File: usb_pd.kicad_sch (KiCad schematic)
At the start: 42 parts, among them J1 USB-C_GCT_USB4105-GF-A, J2 JST_SH_1x4_SM04B-SRSS-TB-LF-SN, Q1 SQS401EN-T1_BE3, U1 STUSB4500_QFN, U5 TVS2200DRVR, U6 TPD4E02B04DQA, U7 TVS2200DRVR, U8 TVS2200DRVR

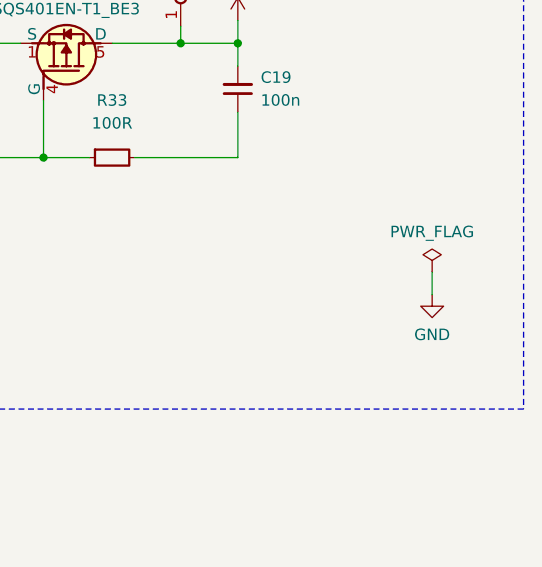
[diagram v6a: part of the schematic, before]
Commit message: [#57764] ADD GND testpoint
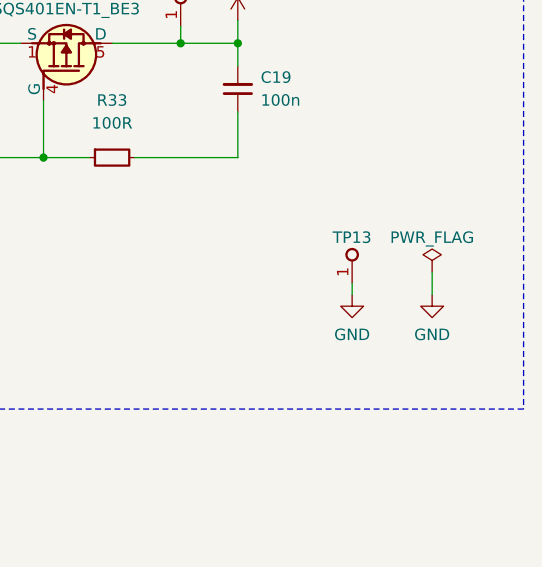
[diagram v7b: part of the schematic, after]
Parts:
- added TP13: TP_0.75mm_SMD, antmicro-footprints:TP_SMD_0.75mm, symbol antmicroTestPoints:TP_0.75mm_SMD
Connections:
- net GND: now also TP13.1
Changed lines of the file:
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@@
     (stroke (width 0) (type default))
   )
+  (wire (pts (xy 339.09 87.63) (xy 339.09 88.9))
+    (stroke (width 0) (type default))
+  )
   (wire (pts (xy 260.35 127) (xy 260.35 130.81))
     (stroke (width 0) (type default))
@@
     )
   )
+  (symbol (lib_id "antmicroTestPoints:TP_0.75mm_SMD") (at 339.09 87.63 90) (unit 1)
+    (in_bom no) (on_board yes) (dnp no)
+    (property "Reference" "TP13" (at 339.09 82.55 90)
+      (effects (font (size 1.27 1.27) (thickness 0.15)))
+    )
+    (property "Value" "TP_0.75mm_SMD" (at 342.9 76.835 0)
+      (effects (font (size 1.27 1.27) (thickness 0.15)) (justify left bottom) hide)
+    )
+    (property "Footprint" "antmicro-footprints:TP_SMD_0.75mm" (at 345.44 76.835 0)
+      (effects (font (size 1.27 1.27) (thickness 0.15)) (justify left bottom) hide)
+    )
+    (property "Datasheet" "" (at 351.79 69.85 0)
+      (effects (font (size 1.27 1.27) (thickness 0.15)) (justify left bottom) hide)
+    )
+    (property "MPN" "" (at 350.52 76.835 0)
+      (effects (font (size 1.27 1.27) (thickness 0.15)) (justify left bottom) hide)
+    )
+    (property "Manufacturer" "" (at 345.44 76.835 0)
+      (effects (font (size 1.27 1.27) (thickness 0.15)) (justify left bottom) hide)
+    )
+    (property "Author" "Antmicro" (at 347.98 76.835 0)
+      (effects (font (size 1.27 1.27) (thickness 0.15)) (justify left bottom) hide)
+    )
+    (property "License" "Apache-2.0" (at 350.52 76.835 0)
+      (effects (font (size 1.27 1.27) (thickness 0.15)) (justify left bottom) hide)
+    )
+    (pin "1")
+    (instances
+      (project "USB-C-power-adapter"
+        (path "/8da33aa8-79ed-467a-95ed-bf58aa0d1db6/344e016f-20ec-4e27-ac78-d9a1e9a3533b"
+          (reference "TP13") (unit 1)
+        )
+      )
+    )
+  )
   (symbol (lib_id "antmicropower:VBUS") (at 106.68 81.28 0) (mirror y) (unit 1)
     (in_bom yes) (on_board yes) (dnp no) (fields_autoplaced)
@@
   )
   (symbol (lib_id "antmicropower:PWR_FLAG") (at 347.98 86.36 0) (unit 1)
-    (in_bom yes) (on_board yes) (dnp no) (fields_autoplaced)
+    (in_bom yes) (on_board yes) (dnp no)
     (property "Reference" "#FLG01" (at 347.98 84.455 0)
       (effects (font (size 1.27 1.27)) hide)
     )
-    (property "Value" "PWR_FLAG" (at 347.98 81.915 0)
+    (property "Value" "PWR_FLAG" (at 347.98 82.55 0)
       (effects (font (size 1.27 1.27)))
     )
@@
         )
       )
+    )
+  )
+  (symbol (lib_id "antmicropower:GND") (at 339.09 88.9 0) (mirror y) (unit 1)
+    (in_bom yes) (on_board yes) (dnp no) (fields_autoplaced)
+    (property "Reference" "#PWR04" (at 330.2 91.44 0)
+      (effects (font (size 1.27 1.27) (thickness 0.15)) (justify left bottom) hide)
+    )
+    (property "Value" "GND" (at 339.09 93.345 0)
+      (effects (font (size 1.27 1.27) (thickness 0.15)))
+    )
+    (property "Footprint" "" (at 330.2 96.52 0)
+      (effects (font (size 1.27 1.27) (thickness 0.15)) (justify left bottom) hide)
+    )
+    (property "Datasheet" "" (at 330.2 101.6 0)
+      (effects (font (size 1.27 1.27) (thickness 0.15)) (justify left bottom) hide)
+    )
+    (property "Author" "Antmicro" (at 330.2 96.52 0)
+      (effects (font (size 1.27 1.27) (thickness 0.15)) (justify left bottom) hide)
+    )
+    (property "License" "Apache-2.0" (at 330.2 99.06 0)
+      (effects (font (size 1.27 1.27) (thickness 0.15)) (justify left bottom) hide)
+    )
+    (pin "1")
+    (instances
+      (project "USB-C-power-adapter"
+        (path "/8da33aa8-79ed-467a-95ed-bf58aa0d1db6/344e016f-20ec-4e27-ac78-d9a1e9a3533b"
+          (reference "#PWR04") (unit 1)
+        )
+      )

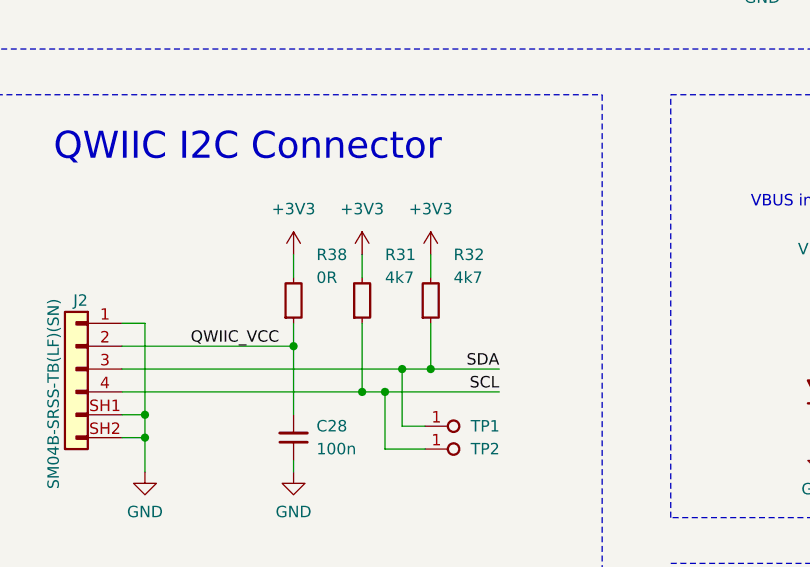
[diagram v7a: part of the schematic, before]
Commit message: [#57225] Improve Vbus, add output caps to layout
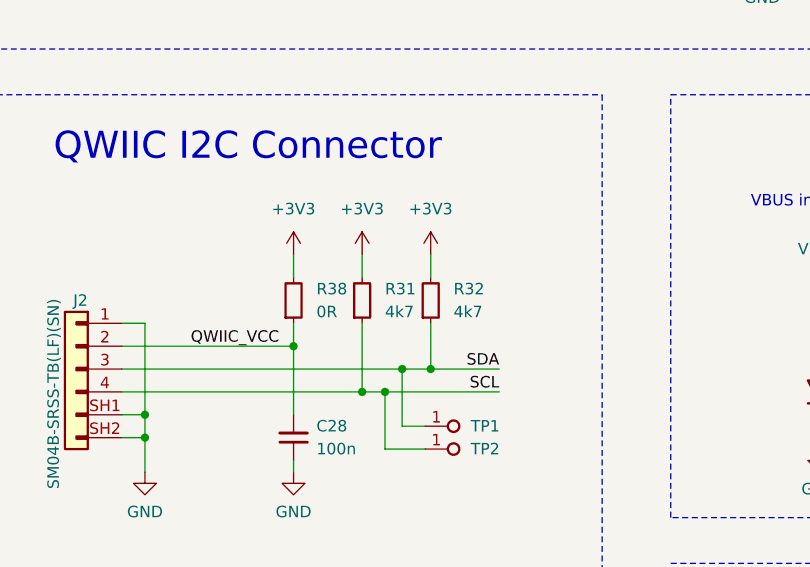
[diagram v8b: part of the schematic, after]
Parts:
- removed R38: R_0R_0603, antmicro-footprints:R_0603_1608Metric, symbol antmicroResistors0603:R_0R_0603
- added R38: R_0R_0402, antmicro-footprints:R_0402_1005Metric, symbol antmicroResistors0402:R_0R_0402
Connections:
- net +3V3: now also R38.2
- net QWIIC_VCC: now also R38.1
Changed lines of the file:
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@@
   )
   (symbol (lib_id "antmicroResistors0402:R_4k7_0402") (at 171.45 132.08 90) (unit 1)
-    (in_bom yes) (on_board yes) (dnp no)
-    (property "Reference" "R31" (at 173.99 124.46 90)
+    (in_bom yes) (on_board yes) (dnp no) (fields_autoplaced)
+    (property "Reference" "R31" (at 173.99 128.27 90)
       (effects (font (size 1.27 1.27) (thickness 0.15)) (justify right))
     )
@@
       (effects (font (size 1.27 1.27) (thickness 0.15)) (justify left bottom) hide)
     )
-    (property "Val" "4k7" (at 173.99 127 90)
+    (property "Val" "4k7" (at 173.99 130.81 90)
       (effects (font (size 1.27 1.27) (thickness 0.15)) (justify right))
     )
@@
   )
   (symbol (lib_id "antmicroResistors0402:R_4k7_0402") (at 179.07 132.08 90) (unit 1)
-    (in_bom yes) (on_board yes) (dnp no)
-    (property "Reference" "R32" (at 181.61 124.46 90)
+    (in_bom yes) (on_board yes) (dnp no) (fields_autoplaced)
+    (property "Reference" "R32" (at 181.61 128.27 90)
       (effects (font (size 1.27 1.27) (thickness 0.15)) (justify right))
     )
@@
       (effects (font (size 1.27 1.27) (thickness 0.15)) (justify left bottom) hide)
     )
-    (property "Val" "4k7" (at 181.61 127 90)
+    (property "Val" "4k7" (at 181.61 130.81 90)
       (effects (font (size 1.27 1.27) (thickness 0.15)) (justify right))
     )
@@
         (path "/8da33aa8-79ed-467a-95ed-bf58aa0d1db6/344e016f-20ec-4e27-ac78-d9a1e9a3533b"
           (reference "J2") (unit 1)
-        )
-      )
-    )
-  )
-  (symbol (lib_id "antmicroResistors0603:R_0R_0603") (at 163.83 132.08 90) (unit 1)
-    (in_bom yes) (on_board yes) (dnp no)
-    (property "Reference" "R38" (at 166.37 124.46 90)
-      (effects (font (size 1.27 1.27) (thickness 0.15)) (justify right))
-    )
-    (property "Value" "R_0R_0603" (at 176.53 111.76 0)
-      (effects (font (size 1.27 1.27) (thickness 0.15)) (justify left bottom) hide)
-    )
-    (property "Footprint" "antmicro-footprints:R_0603_1608Metric" (at 179.07 111.76 0)
-      (effects (font (size 1.27 1.27) (thickness 0.15)) (justify left bottom) hide)
-    )
-    (property "Datasheet" "https://www.bourns.com/docs/product-datasheets/cr.pdf?sfvrsn=574d41f6_14" (at 181.61 111.76 0)
-      (effects (font (size 1.27 1.27) (thickness 0.15)) (justify left bottom) hide)
-    )
-    (property "MPN" "CR0603-J/-000ELF" (at 184.15 111.76 0)
-      (effects (font (size 1.27 1.27) (thickness 0.15)) (justify left bottom) hide)
-    )
-    (property "Manufacturer" "Bourns" (at 186.69 111.76 0)
-      (effects (font (size 1.27 1.27) (thickness 0.15)) (justify left bottom) hide)
-    )
-    (property "License" "Apache-2.0" (at 189.23 111.76 0)
-      (effects (font (size 1.27 1.27) (thickness 0.15)) (justify left bottom) hide)
-    )
-    (property "Author" "Antmicro" (at 191.77 111.76 0)
-      (effects (font (size 1.27 1.27) (thickness 0.15)) (justify left bottom) hide)
-    )
-    (property "Val" "0R" (at 166.37 127 90)
-      (effects (font (size 1.27 1.27) (thickness 0.15)) (justify right))
-    )
-    (property "Tolerance" "~" (at 173.99 111.76 0)
-      (effects (font (size 1.27 1.27)) (justify left bottom) hide)
-    )
-    (property "Current" "1A" (at 194.31 111.76 0)
-      (effects (font (size 1.27 1.27) (thickness 0.15)) (justify left bottom) hide)
-    )
-    (pin "2")
-    (pin "1")
-    (instances
-      (project "USB-C-power-adapter"
-        (path "/8da33aa8-79ed-467a-95ed-bf58aa0d1db6/344e016f-20ec-4e27-ac78-d9a1e9a3533b"
-          (reference "R38") (unit 1)
         )
       )
@@
         )
       )
+    )
+  )
+  (symbol (lib_id "antmicroResistors0402:R_0R_0402") (at 163.83 132.08 90) (unit 1)
+    (in_bom yes) (on_board yes) (dnp no) (fields_autoplaced)
+    (property "Reference" "R38" (at 166.37 128.27 90)
+      (effects (font (size 1.27 1.27) (thickness 0.15)) (justify right))
+    )
+    (property "Value" "R_0R_0402" (at 176.53 111.76 0)
+      (effects (font (size 1.27 1.27) (thickness 0.15)) (justify left bottom) hide)
+    )
+    (property "Footprint" "antmicro-footprints:R_0402_1005Metric" (at 179.07 111.76 0)
+      (effects (font (size 1.27 1.27) (thickness 0.15)) (justify left bottom) hide)
+    )
+    (property "Datasheet" "https://industrial.panasonic.com/cdbs/www-data/pdf/RDA0000/AOA0000C301.pdf" (at 181.61 111.76 0)
+      (effects (font (size 1.27 1.27) (thickness 0.15)) (justify left bottom) hide)
+    )
+    (property "MPN" "ERJ2GE0R00X" (at 184.15 111.76 0)
+      (effects (font (size 1.27 1.27) (thickness 0.15)) (justify left bottom) hide)
+    )
+    (property "Manufacturer" "Panasonic" (at 186.69 111.76 0)
+      (effects (font (size 1.27 1.27) (thickness 0.15)) (justify left bottom) hide)
+    )
+    (property "License" "Apache-2.0" (at 189.23 111.76 0)
+      (effects (font (size 1.27 1.27) (thickness 0.15)) (justify left bottom) hide)
+    )
+    (property "Author" "Antmicro" (at 191.77 111.76 0)
+      (effects (font (size 1.27 1.27) (thickness 0.15)) (justify left bottom) hide)
+    )
+    (property "Val" "0R" (at 166.37 130.81 90)
+      (effects (font (size 1.27 1.27) (thickness 0.15)) (justify right))
+    )
+    (property "Tolerance" "~" (at 173.99 111.76 0)
+      (effects (font (size 1.27 1.27)) (justify left bottom) hide)
+    )
+    (property "Current" "1A" (at 194.31 111.76 0)
+      (effects (font (size 1.27 1.27) (thickness 0.15)) (justify left bottom) hide)
+    )
+    (property "DNP" "" (at 163.83 132.08 0)
+      (effects (font (size 1.27 1.27)))
+    )
+    (pin "1")
+    (pin "2")
+    (instances
+      (project "USB-C-power-adapter"
+        (path "/8da33aa8-79ed-467a-95ed-bf58aa0d1db6/344e016f-20ec-4e27-ac78-d9a1e9a3533b"
+          (reference "R38") (unit 1)
+        )
+      )
